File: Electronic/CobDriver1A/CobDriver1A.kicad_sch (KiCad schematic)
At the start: 9 parts, among them J1 Conn02_Pin, J2 Conn02_Pin, U1 AL8860WT-7

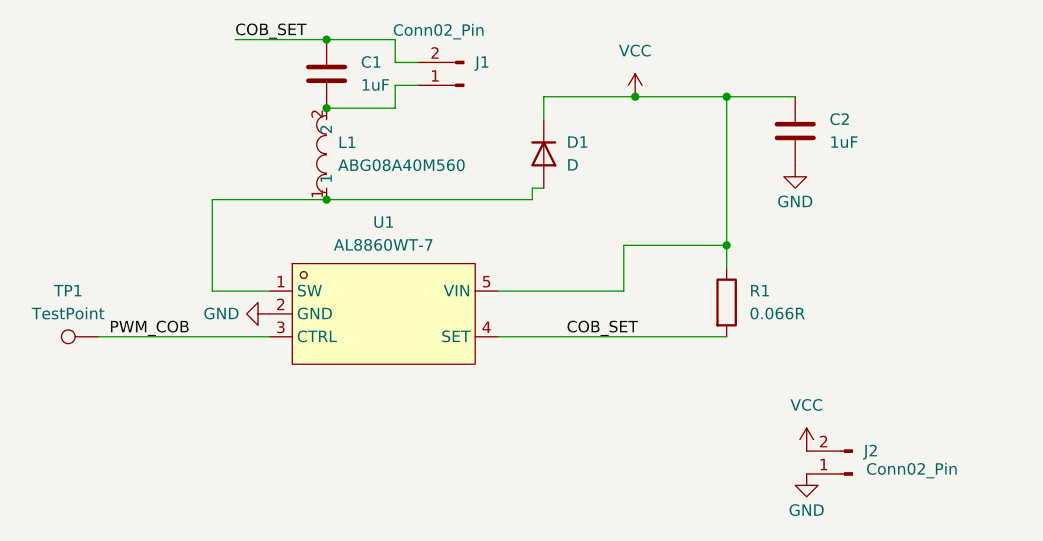
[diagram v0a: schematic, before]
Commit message: CobDriver1A done
- Smaller inductor
- Bigger PCB
- BOM completed
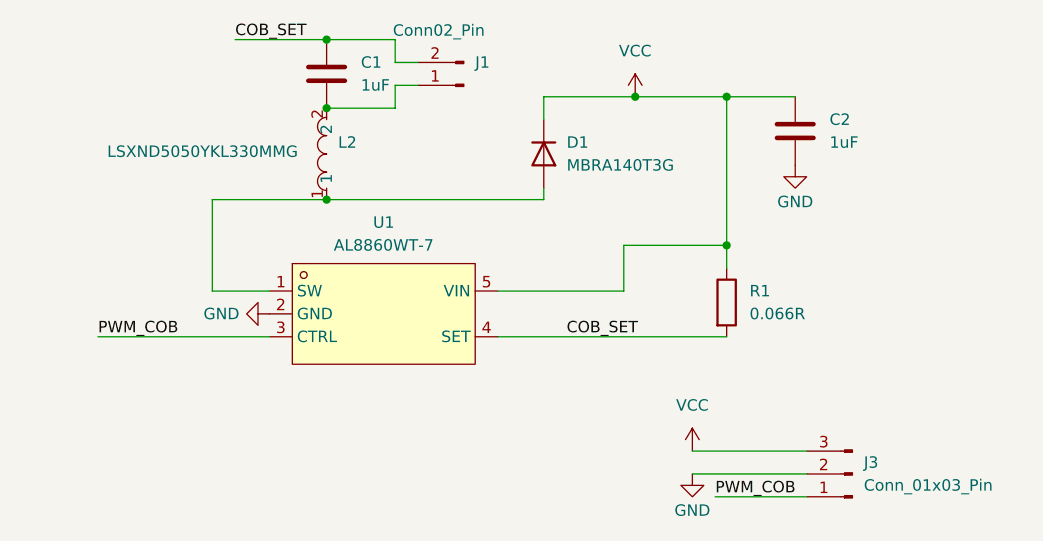
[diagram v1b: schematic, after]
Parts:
- removed J2: Conn02_Pin, Connector_PinSocket_2.54mm:PinSocket_1x02_P2.54mm_Vertical, symbol Connector:Conn_01x02_Pin
- removed L1: ABG08A40M560, lcsc:IND-SMD_L8.0-W8.0_ABG08A40, symbol lcsc:ABG08A40M560
- removed TP1: TestPoint, TestPoint:TestPoint_Pad_D1.5mm, symbol Connector:TestPoint
- added J3: Conn_01x03_Pin, Connector_PinSocket_2.54mm:PinSocket_1x03_P2.54mm_Vertical, symbol Connector:Conn_01x03_Pin
- added L2: LSXND5050YKL330MMG, lcsc:IND-SMD_L4.9-W4.9_LSXND5050, symbol lcsc:LSXND5050YKL330MMG
- C1, C2: LCSC Part (none) -> C49333228
- D1: value D -> MBRA140T3G; LCSC Part (none) -> C54798
- R1: footprint Resistor_SMD:R_0402_1005Metric -> Resistor_SMD:R_0603_1608Metric
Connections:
- net GND: now also J3.2 (Pin_2)
- net PWM_COB: now also J3.1 (Pin_1)
- net VCC: now also J3.3 (Pin_3)
- net at D1.2 (A), U1.1 (SW): now also L2.1
- net at C1.2, J1.1 (Pin_1): now also L2.2
